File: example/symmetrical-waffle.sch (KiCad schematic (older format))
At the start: 0 parts

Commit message: Starting to add the arduino
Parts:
- added C? (x3): 1nF, symbol C
- added C? (x2): 22pF, symbol C
- added U?: ATMEGA328-AU, Housings_QFP:TQFP-32_7x7mm_Pitch0.8mm, symbol ATMEGA328-AU
- added Y?: Crystal, symbol Crystal
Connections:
- net GND: now also C?.1, C?.1, C?.2, C?.2, C?.2, U?.21 (GND), U?.3 (GND), U?.5 (GND)
- net VCC: now also C?.1, C?.1, U?.18 (AVCC), U?.4 (VCC), U?.6 (VCC)
- new net: C?.1, U?.20 (AREF)
- new net: C?.2, U?.7 ((PCINT6/XTAL1/TOSC1)PB6), Y?.2
- new net: C?.2, U?.8 ((PCINT7/XTAL2/TOSC2)PB7), Y?.1
- no-connect marks 0 -> 2
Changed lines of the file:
@@
 F4 "Signal" I R 2750 1450 60
 $EndSheet
-Wire Wire Line
-	2750 1650 2850 1650
-Wire Wire Line
-	2850 1650 2850 1700
-Wire Wire Line
-	2750 1250 2850 1250
-Wire Wire Line
-	2850 1250 2850 1200
 $Comp
 L GND #PWR?
@@
 Text Label 2850 1450 0    60   ~ 0
 LEDSignal
-Wire Wire Line
-	2750 1450 2850 1450
-Wire Notes Line
-	700  700  3400 700
-Wire Notes Line
-	3400 700  3400 2200
-Wire Notes Line
-	3400 2200 700  2200
-Wire Notes Line
-	700  2200 700  700
 Text Notes 3350 2150 2    60   ~ 0
 Ring of LEDs
+$Comp
+L ATMEGA328-AU U?
+U 1 1 5AA44AB3
+P 2950 5350
+F 0 "U?" H 2200 6600 50  0000 L BNN
+F 1 "ATMEGA328-AU" H 3350 3950 50  0000 L BNN
+F 2 "Housings_QFP:TQFP-32_7x7mm_Pitch0.8mm" H 2950 5350 50  0001 C CIN
+F 3 "" H 2950 5350 50  0001 C CNN
+	1    2950 5350
+	1    0    0    -1
+$EndComp
+$Comp
+L GND #PWR?
+U 1 1 5AA44C73
+P 1850 6750
+F 0 "#PWR?" H 1850 6500 50  0001 C CNN
+F 1 "GND" H 1850 6600 50  0000 C CNN
+F 2 "" H 1850 6750 50  0001 C CNN
+F 3 "" H 1850 6750 50  0001 C CNN
+	1    1850 6750
+	1    0    0    -1
+$EndComp
+$Comp
+L C C?
+U 1 1 5AA44DB8
+P 1450 4600
+F 0 "C?" H 1475 4700 50  0000 L CNN
+F 1 "1nF" H 1475 4500 50  0000 L CNN
+F 2 "" H 1488 4450 50  0001 C CNN
+F 3 "" H 1450 4600 50  0001 C CNN
+	1    1450 4600
+	1    0    0    -1
+$EndComp
+$Comp
+L C C?
+U 1 1 5AA44E41
+P 1200 4600
+F 0 "C?" H 1225 4700 50  0000 L CNN
+F 1 "1nF" H 1225 4500 50  0000 L CNN
+F 2 "" H 1238 4450 50  0001 C CNN
+F 3 "" H 1200 4600 50  0001 C CNN
+	1    1200 4600
+	1    0    0    -1
+$EndComp
+$Comp
+L VCC #PWR?
+U 1 1 5AA44FFB
+P 1450 4050
+F 0 "#PWR?" H 1450 3900 50  0001 C CNN
+F 1 "VCC" H 1450 4200 50  0000 C CNN
+F 2 "" H 1450 4050 50  0001 C CNN
+F 3 "" H 1450 4050 50  0001 C CNN
+	1    1450 4050
+	1    0    0    -1
+$EndComp
+$Comp
+L GND #PWR?
+U 1 1 5AA450DB
+P 1450 4950
+F 0 "#PWR?" H 1450 4700 50  0001 C CNN
+F 1 "GND" H 1450 4800 50  0000 C CNN
+F 2 "" H 1450 4950 50  0001 C CNN
+F 3 "" H 1450 4950 50  0001 C CNN
+	1    1450 4950
+	1    0    0    -1
+$EndComp
+NoConn ~ 2050 5600
+NoConn ~ 2050 5700
+$Comp
+L C C?
+U 1 1 5AA451F3
+P 1850 5200
+F 0 "C?" H 1875 5300 50  0000 L CNN
+F 1 "1nF" H 1875 5100 50  0000 L CNN
+F 2 "" H 1888 5050 50  0001 C CNN
+F 3 "" H 1850 5200 50  0001 C CNN
+	1    1850 5200
+	1    0    0    -1
+$EndComp
+$Comp
+L Crystal Y?
+U 1 1 5AA45383
+P 4900 5100
+F 0 "Y?" V 4900 5250 50  0000 C CNN
+F 1 "Crystal" V 4900 4850 50  0000 C CNN
+F 2 "" H 4900 5100 50  0001 C CNN
+F 3 "" H 4900 5100 50  0001 C CNN
+	1    4900 5100
+	0    -1   -1   0
+$EndComp
+Wire Wire Line
+	2750 1650 2850 1650
+Wire Wire Line
+	2850 1650 2850 1700
+Wire Wire Line
+	2750 1250 2850 1250
+Wire Wire Line
+	2850 1250 2850 1200
+Wire Wire Line
+	2750 1450 2850 1450
+Wire Notes Line
+	700  700  3400 700
+Wire Notes Line
+	3400 700  3400 2200
+Wire Notes Line
+	3400 2200 700  2200
+Wire Notes Line
+	700  2200 700  700
+Wire Wire Line
+	2050 6350 1850 6350
+Wire Wire Line
+	1850 5350 1850 6350
+Wire Wire Line
+	1850 6350 1850 6450
+Wire Wire Line
+	1850 6450 1850 6550
+Wire Wire Line
+	1850 6550 1850 6750
+Wire Wire Line
+	1850 6450 2050 6450
+Wire Wire Line
+	1850 6550 2050 6550
+Connection ~ 1850 6450
+Connection ~ 1850 6550
+Wire Wire Line
+	1200 4350 1450 4350
+Wire Wire Line
+	1450 4350 1850 4350
+Wire Wire Line
+	1850 4350 2050 4350
+Wire Wire Line
+	1200 4350 1200 4450
+Connection ~ 1450 4350
+Wire Wire Line
+	1850 4550 2050 4550
+Connection ~ 1850 4350
+Wire Wire Line
+	1450 4050 1450 4350
+Wire Wire Line
+	1450 4350 1450 4450
+Wire Wire Line
+	1850 4250 1850 4350
+Wire Wire Line
+	1850 4350 1850 4550
+Wire Wire Line
+	1850 4250 2050 4250
+Wire Wire Line
+	1200 4750 1200 4850
+Wire Wire Line
+	1200 4850 1450 4850
+Wire Wire Line
+	1450 4750 1450 4850
+Wire Wire Line
+	1450 4850 1450 4950
+Connection ~ 1450 4850
+Wire Wire Line
+	2050 4850 1850 4850
+Wire Wire Line
+	1850 4850 1850 5050
+Connection ~ 1850 6350
+Wire Wire Line
+	3950 4850 4900 4850
+Wire Wire Line
+	4550 5350 4550 4950
+Wire Wire Line
+	4550 4950 3950 4950
+Wire Wire Line
+	5000 4750 4900 4750
+Wire Wire Line
+	4900 4750 4900 4850
+Wire Wire Line
+	4900 4850 4900 4950
+Connection ~ 4900 4850
+Wire Wire Line
+	4550 5350 4900 5350
+Wire Wire Line
+	4900 5250 4900 5350
+Wire Wire Line
+	4900 5350 4900 5450
+Wire Wire Line
+	4900 5450 5000 5450
+Connection ~ 4900 5350
+Wire Wire Line
+	5300 5450 5500 5450
+Wire Wire Line
+	5500 4750 5500 5450
+Wire Wire Line
+	5500 5450 5500 5550
+Wire Wire Line
+	5500 4750 5300 4750
+Connection ~ 5500 5450
+$Comp
+L GND #PWR?
+U 1 1 5AA45C56
+P 5500 5550
+F 0 "#PWR?" H 5500 5300 50  0001 C CNN
+F 1 "GND" H 5500 5400 50  0000 C CNN
+F 2 "" H 5500 5550 50  0001 C CNN
+F 3 "" H 5500 5550 50  0001 C CNN
+	1    5500 5550
+	1    0    0    -1
+$EndComp
+$Comp
+L C C?
+U 1 1 5AA45D60
+P 5150 4750
+F 0 "C?" V 5200 4800 50  0000 L CNN
+F 1 "22pF" V 5100 4800 50  0000 L CNN
+F 2 "" H 5188 4600 50  0001 C CNN
+F 3 "" H 5150 4750 50  0001 C CNN
+	1    5150 4750
+	0    1    1    0
+$EndComp
+$Comp
+L C C?
+U 1 1 5AA45E63
+P 5150 5450
+F 0 "C?" V 5200 5500 50  0000 L CNN
+F 1 "22pF" V 5100 5500 50  0000 L CNN
+F 2 "" H 5188 5300 50  0001 C CNN
+F 3 "" H 5150 5450 50  0001 C CNN
+	1    5150 5450
+	0    1    1    0
+$EndComp
 $EndSCHEMATC

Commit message: Finishing the basic schematic
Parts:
- removed C?: 22pF, symbol C
- added C?: 22pF, symbol C
- added C?: 100nF, symbol C
- added J?: ICSP, symbol Conn_02x03_Odd_Even
- added J?: FTDI Programmer, symbol Conn_01x06
- added R?: 10K, symbol R
- added SW?: SW_Push, symbol SW_Push
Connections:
- net GND: now also C?.1, J?.5 (Pin_5), J?.6 (Pin_6), J?.6 (Pin_6), SW?.2
- net LEDSignal: now also U?.23 ((PCINT8/ADC0)PC0)
- net MOSI: now reaches U?.15 ((PCINT3/OC2A/MOSI)PB3)
- net MOSI: now also J?.4 (Pin_4)
- net MISO: now reaches U?.16 ((PCINT4/MISO)PB4)
- net MISO: now also J?.1 (Pin_1)
- net SCK: now reaches U?.17 ((PCINT5/SCK)PB5)
- net SCK: now also J?.3 (Pin_3)
- net RST_CIRCUIT: now reaches U?.29 ((PCINT14/~RESET~)PC6)
- net RST_CIRCUIT: now also C?.2, J?.5 (Pin_5), R?.2, SW?.1
- net XTAL2: now reaches C?.2, Y?.2
- net XTAL2: now also U?.8 ((PCINT7/XTAL2/TOSC2)PB7); no longer U?.7 ((PCINT6/XTAL1/TOSC1)PB6)
- net XTAL1: now reaches Y?.1
- net XTAL1: now also U?.7 ((PCINT6/XTAL1/TOSC1)PB6), C?.2; no longer U?.8 ((PCINT7/XTAL2/TOSC2)PB7)
- new net +5V: J?.2 (Pin_2), J?.4 (Pin_4), R?.1
- new net DTR: C?.1, J?.1 (Pin_1)
- new net RX: J?.3 (Pin_3)
- new net TX: J?.2 (Pin_2)
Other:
- note added: "Bootloader Programmer"
- note added: "Clock Circuit"
- note added: "Reset Logic"
- note added: "Serial Programmer\n"
- moved on the sheet: C?, U?, Y?

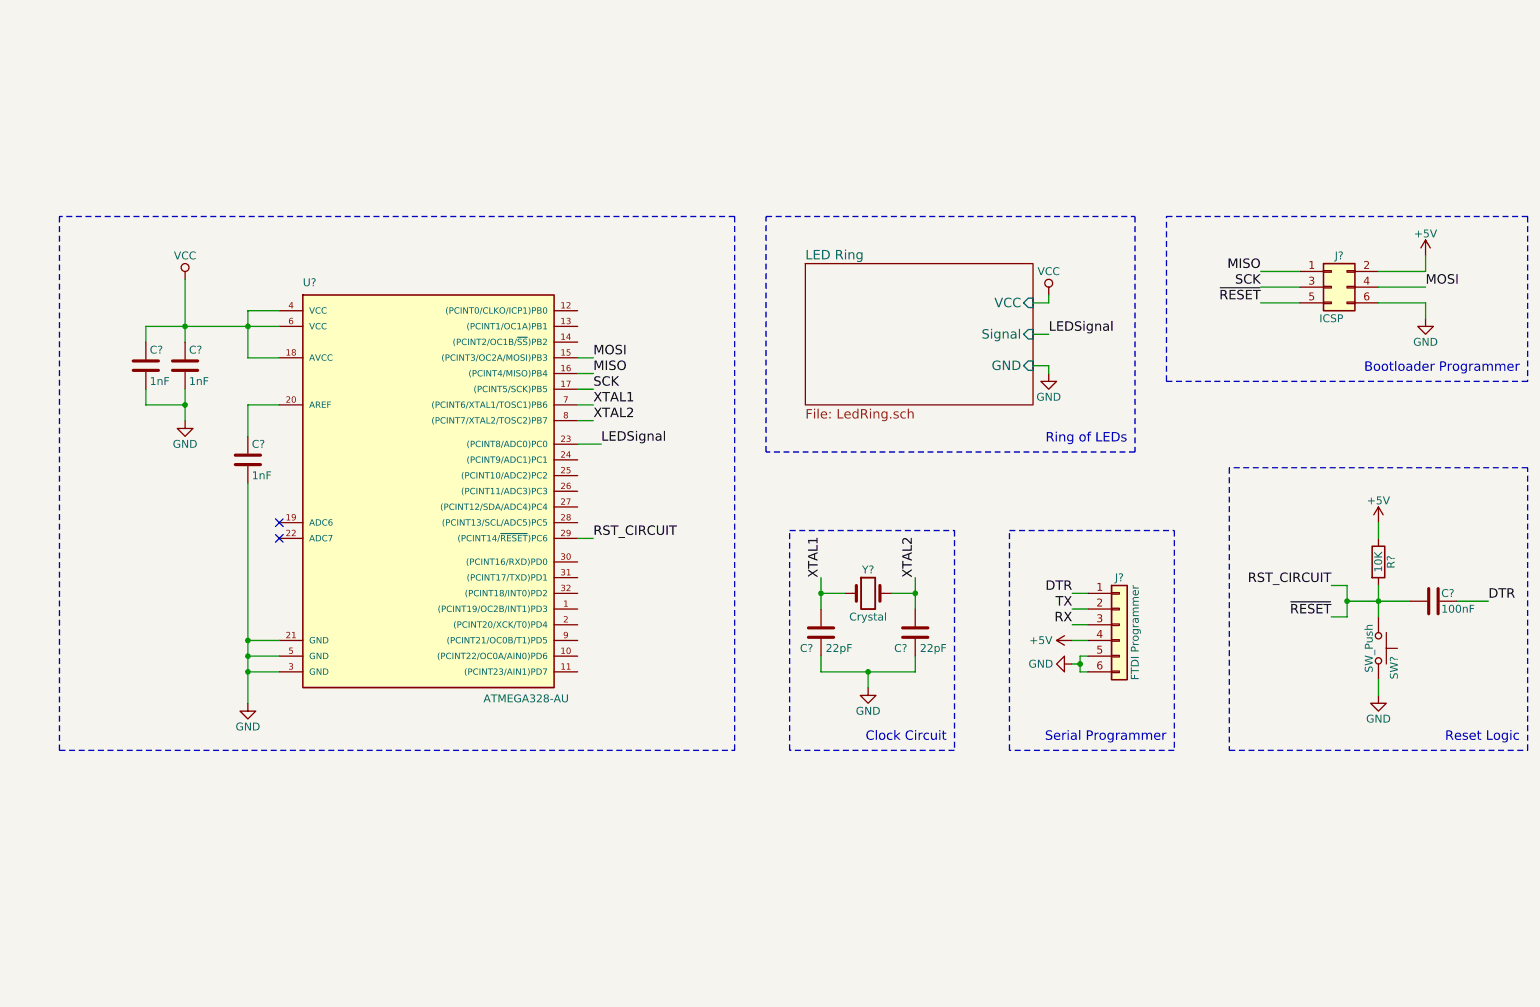
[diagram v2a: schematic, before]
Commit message: Adding a power switch and GPIO header
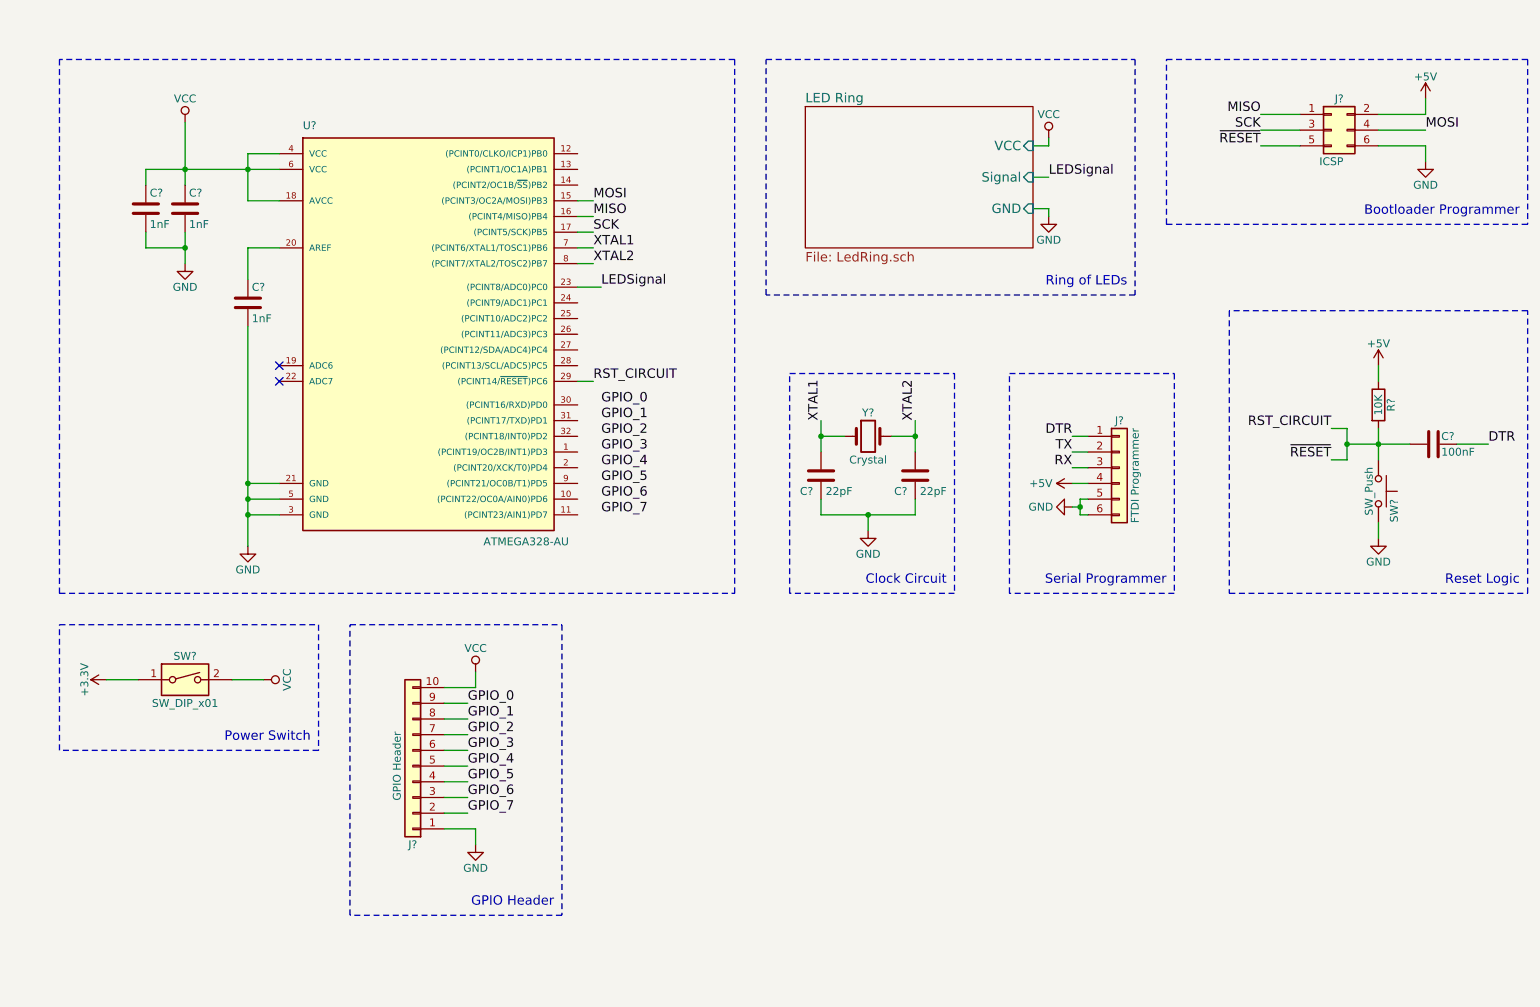
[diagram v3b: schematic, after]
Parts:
- added J?: GPIO Header, symbol Conn_01x10
- added SW?: SW_DIP_x01, symbol SW_DIP_x01
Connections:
- net GND: now also J?.1 (Pin_1)
- net VCC: now also J?.10 (Pin_10), SW?.2
- new net +3V3: SW?.1
- new net GPIO_0: J?.9 (Pin_9)
- new net GPIO_1: J?.8 (Pin_8)
- new net GPIO_2: J?.7 (Pin_7)
- new net GPIO_3: J?.6 (Pin_6)
- new net GPIO_4: J?.5 (Pin_5)
- new net GPIO_5: J?.4 (Pin_4)
- new net GPIO_6: J?.3 (Pin_3)
- new net GPIO_7: J?.2 (Pin_2)
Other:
- note added: "GPIO Header"
- note added: "Power Switch"
- moved on the sheet: C?, J?, R?, SW?, U?, Y?

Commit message: Reannotating
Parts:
- C1, C2, C3, C4, C5, C6: renamed from C?; footprint (none) -> Capacitors_SMD:C_0805
- J1: renamed from J?; footprint (none) -> Pin_Headers:Pin_Header_Angled_2x03_Pitch1.00mm
- J2: renamed from J?; footprint (none) -> Pin_Headers:Pin_Header_Angled_1x06_Pitch1.00mm
- J3: renamed from J?; footprint (none) -> Pin_Headers:Pin_Header_Straight_1x10_Pitch1.00mm
- R1: renamed from R?; footprint (none) -> Resistors_SMD:R_0805
- SW1: renamed from SW?; footprint (none) -> Buttons_Switches_THT:SW_PUSH_6mm_h5mm
- SW2: renamed from SW?; footprint (none) -> Buttons_Switches_THT:SW_DIP_x1_W7.62mm_Piano
- Y1: renamed from Y?; footprint (none) -> Crystals:Crystal_AT310_d3.0mm_l10.0mm_Horizontal
- gave numbers to parts that had none: 1
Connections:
- net GPIO_0: now also U1.30 ((PCINT16/RXD)PD0)
- net GPIO_1: now also U1.31 ((PCINT17/TXD)PD1)
- net GPIO_2: now also U1.32 ((PCINT18/INT0)PD2)
- net GPIO_3: now also U1.1 ((PCINT19/OC2B/INT1)PD3)
- net GPIO_4: now also U1.2 ((PCINT20/XCK/T0)PD4)
- net GPIO_5: now also U1.9 ((PCINT21/OC0B/T1)PD5)
- net GPIO_6: now also U1.10 ((PCINT22/OC0A/AIN0)PD6)
- net GPIO_7: now also U1.11 ((PCINT23/AIN1)PD7)
- no-connect marks 2 -> 10
